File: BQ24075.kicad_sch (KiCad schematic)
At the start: 15 parts, among them U3 BQ24075RGT

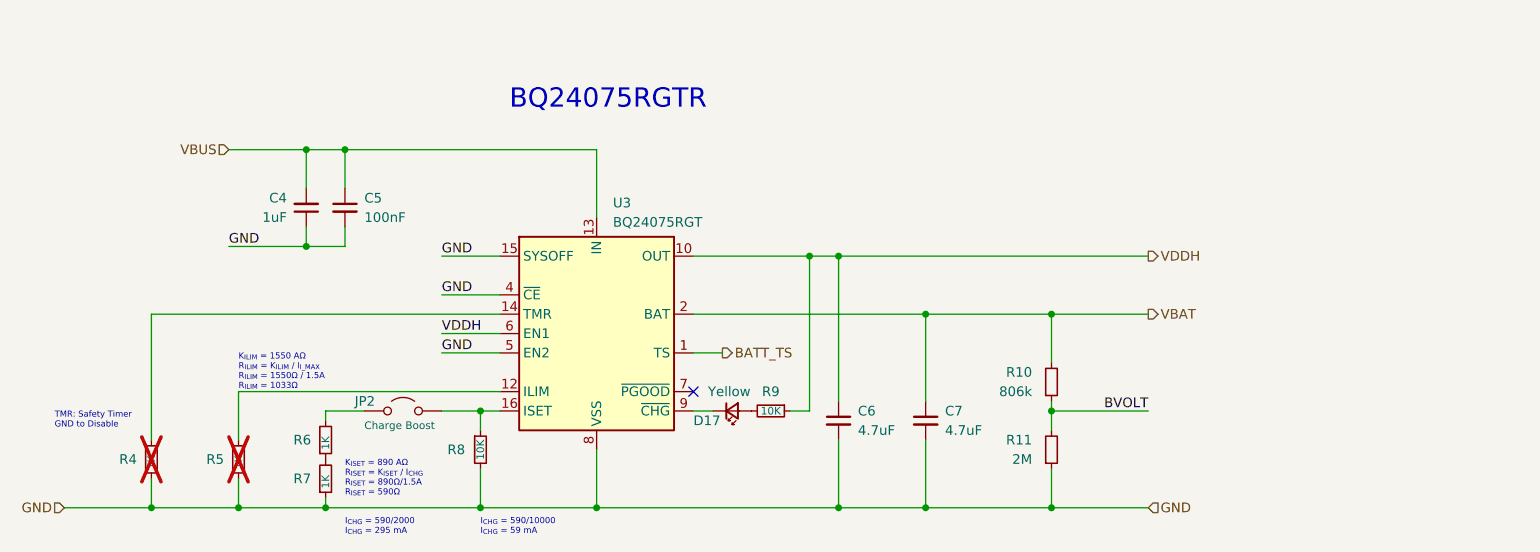
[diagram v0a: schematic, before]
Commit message: Add some todo notes, add 3/2 pin battery connectors
Add NTC connector, Update power scheme for RF module
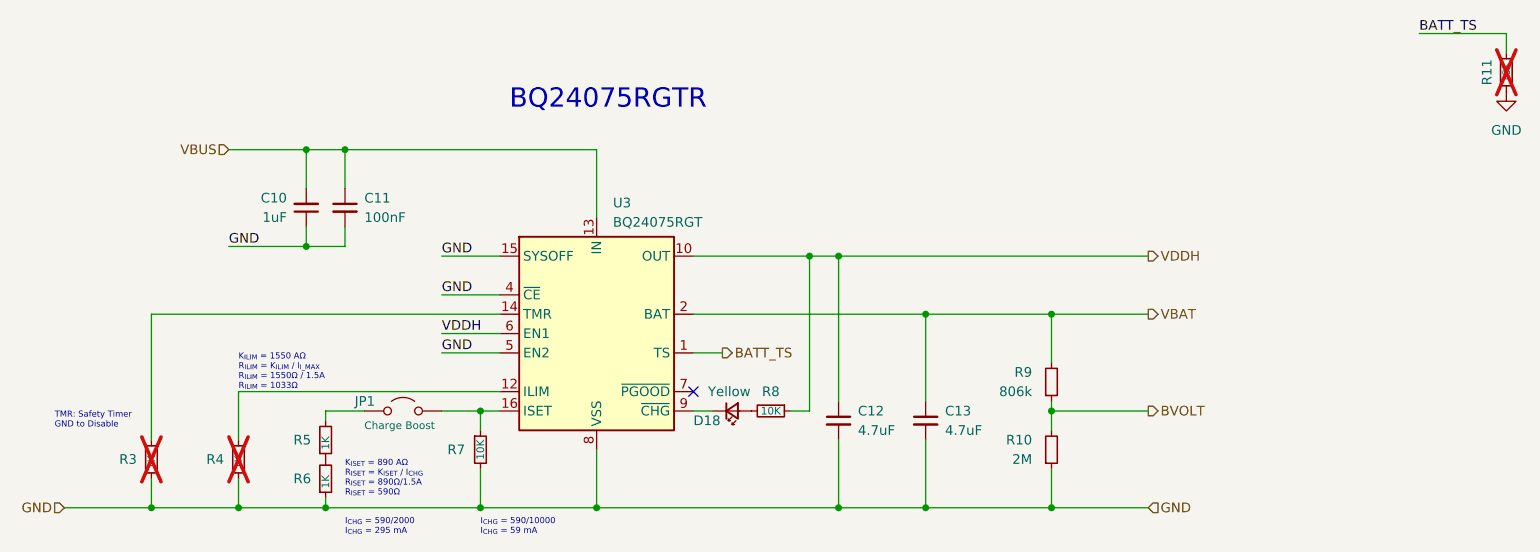
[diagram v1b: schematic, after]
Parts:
- added R11: 10K, Resistor_SMD:R_0603_1608Metric, symbol Device:R_Small
- renumbered C4 to C10, C5 to C11, C6 to C12, C7 to C13, D17 to D18, JP2 to JP1, R11 to R10, R4 to R3, R5 to R4, R6 to R5, R7 to R6, R8 to R7, R9 to R8, R10 to R9
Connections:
- net BATT_TS: now also R11.1
- net GND: now also R11.2

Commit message: Update BOM
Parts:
- removed C12, C13: 4.7uF, Capacitor_SMD:C_0805_2012Metric, symbol Device:C_Small
- added C19: 10uF, Capacitor_SMD:C_0805_2012Metric, symbol Device:C_Small
- C10: Price $0.16 -> $0.10
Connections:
- net GND: now also C19.2
- net VDDH: now also C19.1
- net VBUS renamed V_{BUS}
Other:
- title: (none) -> Crumb Catcher

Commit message: Add some research, update switches
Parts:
- renumbered C10 to C4, C11 to C5, C19 to C6, D18 to D3
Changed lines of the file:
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@@
 		(dnp no)
 		(fields_autoplaced yes)
-		(property "Reference" "C10"
+		(property "Reference" "C4"
 			(at 105.41 67.3035 0)
 			(effects
@@
 			(project "CrumbCatcherLight"
 				(path "/eedae293-eb5b-47bd-b383-bccfdf81bf72/1bafed49-ccd3-4a1b-80c1-5d5289cf9b73"
-					(reference "C10")
+					(reference "C4")
 					(unit 1)
 				)
@@
 		(on_board yes)
 		(dnp no)
-		(property "Reference" "D18"
+		(property "Reference" "D3"
 			(at 158.75 96.52 0)
 			(effects
@@
 			(project "CrumbCatcherLight"
 				(path "/eedae293-eb5b-47bd-b383-bccfdf81bf72/1bafed49-ccd3-4a1b-80c1-5d5289cf9b73"
-					(reference "D18")
+					(reference "D3")
 					(unit 1)
 				)
@@
 		(dnp no)
 		(fields_autoplaced yes)
-		(property "Reference" "C11"
+		(property "Reference" "C5"
 			(at 115.57 67.3162 0)
 			(effects
@@
 			(project "CrumbCatcherLight"
 				(path "/eedae293-eb5b-47bd-b383-bccfdf81bf72/1bafed49-ccd3-4a1b-80c1-5d5289cf9b73"
-					(reference "C11")
+					(reference "C5")
 					(unit 1)
 				)
@@
 		(dnp no)
 		(fields_autoplaced yes)
-		(property "Reference" "C19"
+		(property "Reference" "C6"
 			(at 180.34 95.2562 0)
 			(effects
@@
 			(project "CrumbCatcherLight"
 				(path "/eedae293-eb5b-47bd-b383-bccfdf81bf72/1bafed49-ccd3-4a1b-80c1-5d5289cf9b73"
-					(reference "C19")
+					(reference "C6")
 					(unit 1)
 				)
@@
 		(dnp no)
 		(fields_autoplaced yes)
-		(property "Reference" "#PWR022"
+		(property "Reference" "#PWR018"
 			(at 265.43 59.69 0)
 			(effects
@@
 			(project "CrumbCatcherLight"
 				(path "/eedae293-eb5b-47bd-b383-bccfdf81bf72/1bafed49-ccd3-4a1b-80c1-5d5289cf9b73"
-					(reference "#PWR022")
+					(reference "#PWR018")
 					(unit 1)
 				)
